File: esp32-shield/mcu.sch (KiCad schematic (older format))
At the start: 31 parts, among them J11 DNP, J5 Conn_01x14_Female, J6 Conn_01x14_Female, Q3 S8050, Q4 S8050, SW1 SKRKAEE020, U13 ESP32-WROOM32, U14 W25Q32JVSS, U4 SN74LV1T34DBV, U5 CH340C, U6 AMS1117-3.3, Y1 12MHZ

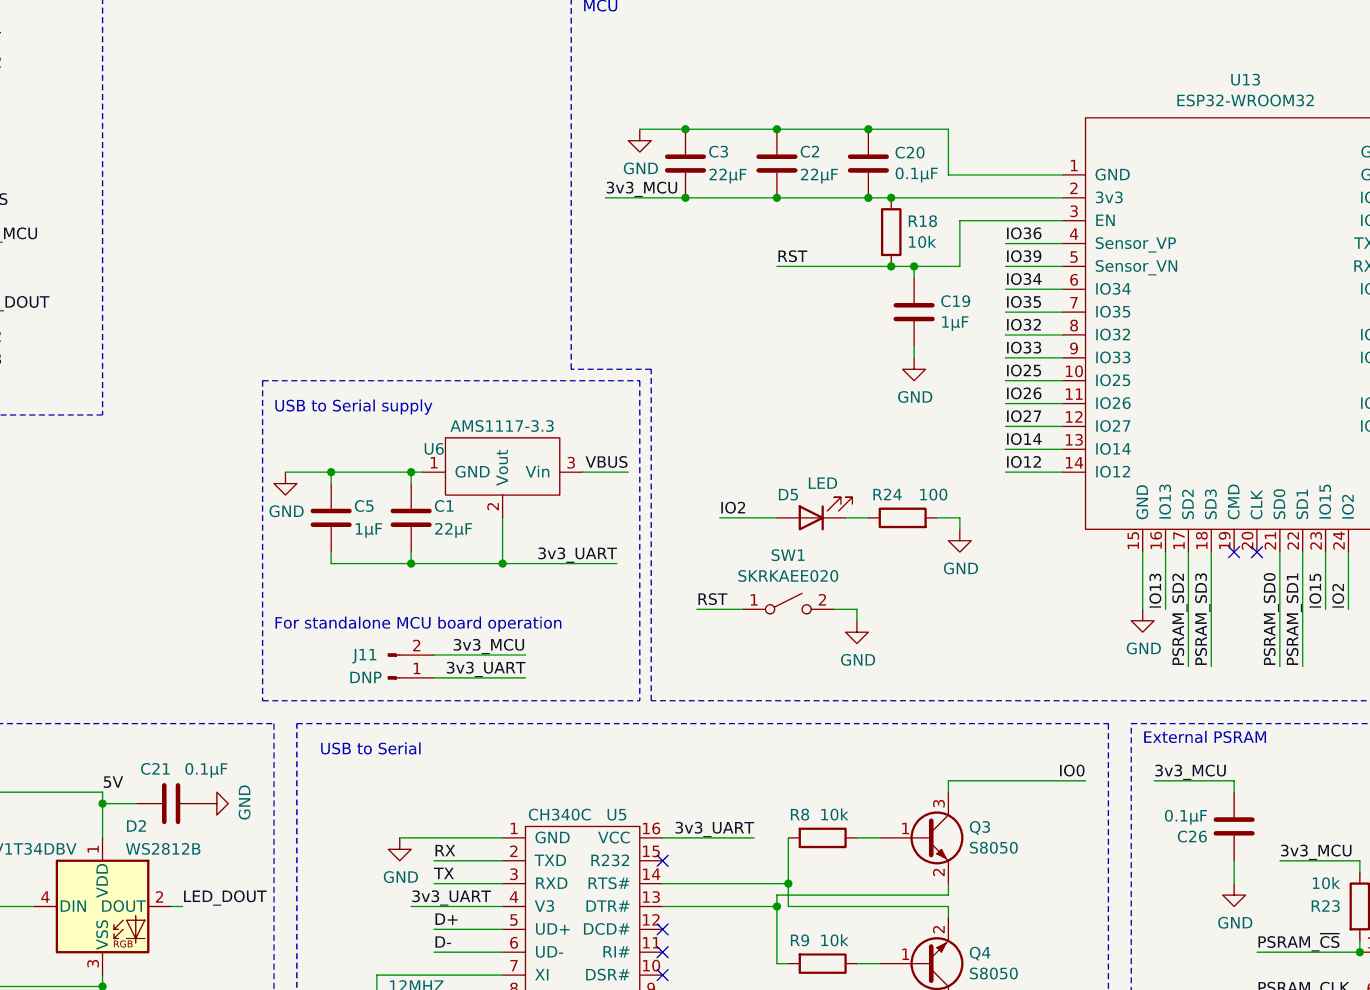
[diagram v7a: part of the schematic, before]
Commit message: swapped .1µ caps for 1µ caps
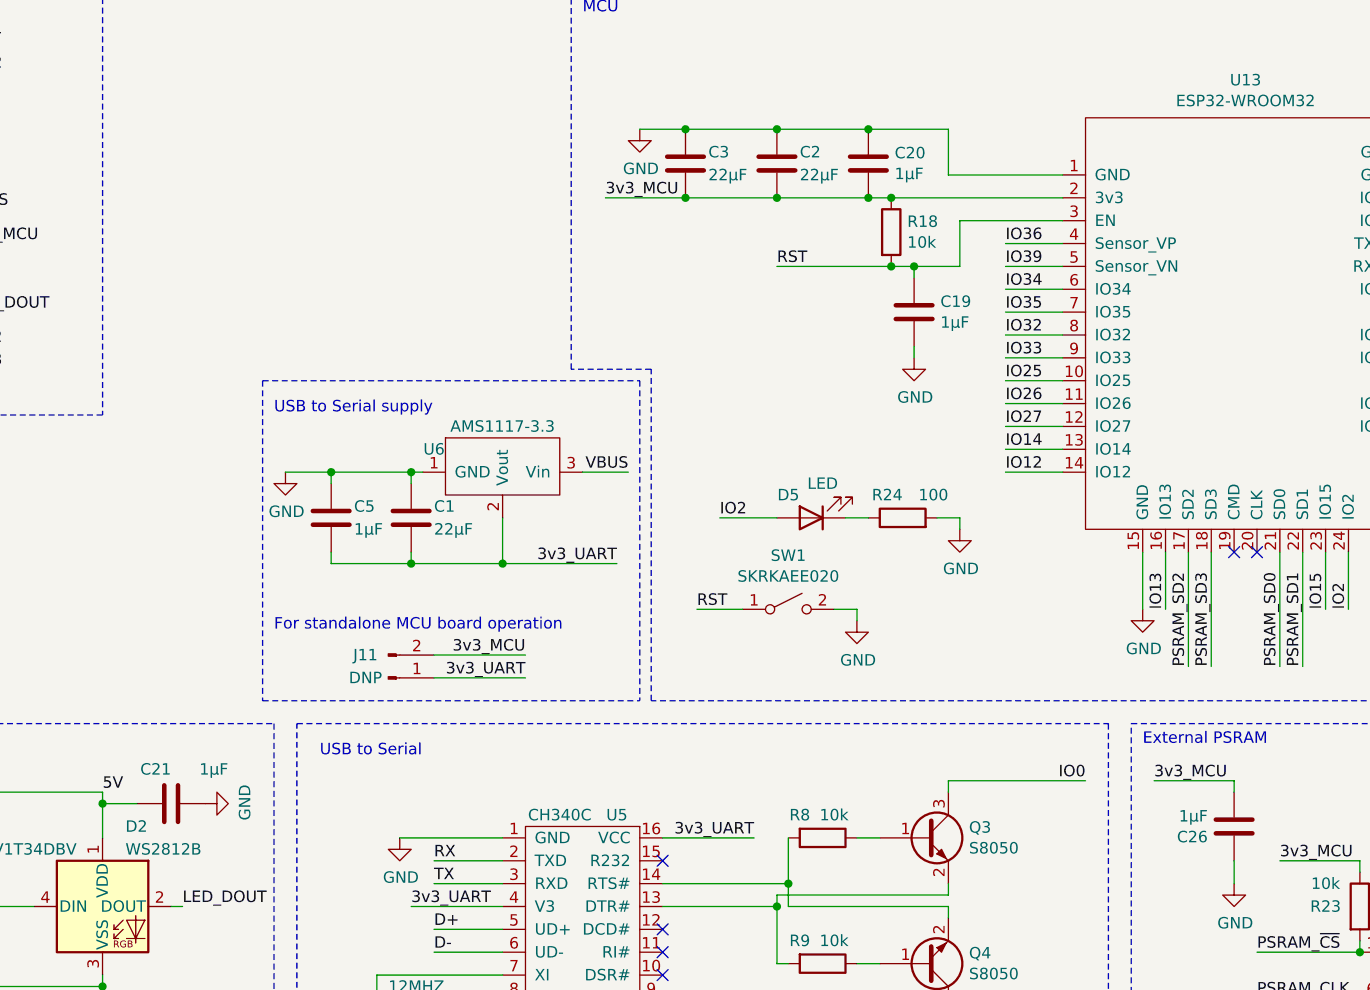
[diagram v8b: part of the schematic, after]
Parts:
- C20, C21, C26: value 0.1µF -> 1µF; LCSC C14858 -> C15849
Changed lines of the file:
@@
 P 5200 1500
 F 0 "C20" H 5315 1546 50  0000 L CNN
-F 1 "0.1µF" H 5315 1455 50  0000 L CNN
+F 1 "1µF" H 5315 1455 50  0000 L CNN
 F 2 "Capacitor_SMD:C_0603_1608Metric_Pad1.05x0.95mm_HandSolder" H 5238 1350 50  0001 C CNN
 F 3 "~" H 5200 1500 50  0001 C CNN
-F 4 "C14858" H 5200 1500 50  0001 C CNN "LCSC"
+F 4 "C15849" H 5200 1500 50  0001 C CNN "LCSC"
 	1    5200 1500
 	1    0    0    -1
@@
 P 6800 4400
 F 0 "C26" H 6915 4446 50  0000 L CNN
-F 1 "0.1µF" H 6915 4355 50  0000 L CNN
+F 1 "1µF" H 6915 4355 50  0000 L CNN
 F 2 "Capacitor_SMD:C_0603_1608Metric_Pad1.05x0.95mm_HandSolder" H 6838 4250 50  0001 C CNN
 F 3 "~" H 6800 4400 50  0001 C CNN
-F 4 "C14858" H 6800 4400 50  0001 C CNN "LCSC"
+F 4 "C15849" H 6800 4400 50  0001 C CNN "LCSC"
 F 5 "DNP" H 6800 4400 50  0001 C CNN "DNP"
 	1    6800 4400
@@
 P 2150 4300
 F 0 "C21" V 2300 4300 50  0000 L CNN
-F 1 "0.1µF" V 2300 4050 50  0000 L CNN
+F 1 "1µF" V 2300 4050 50  0000 L CNN
 F 2 "Capacitor_SMD:C_0603_1608Metric_Pad1.05x0.95mm_HandSolder" H 2188 4150 50  0001 C CNN
 F 3 "~" H 2150 4300 50  0001 C CNN
-F 4 "C14858" H 2150 4300 50  0001 C CNN "LCSC"
+F 4 "C15849" H 2150 4300 50  0001 C CNN "LCSC"
 	1    2150 4300
 	0    -1   -1   0
